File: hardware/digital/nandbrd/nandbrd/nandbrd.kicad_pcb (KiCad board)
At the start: 2 copper layers, 46.9 x 59.8 mm, 4 parts, among them J2 Conn_01x20_Male, U1 MT29F1G08ABAEAWP

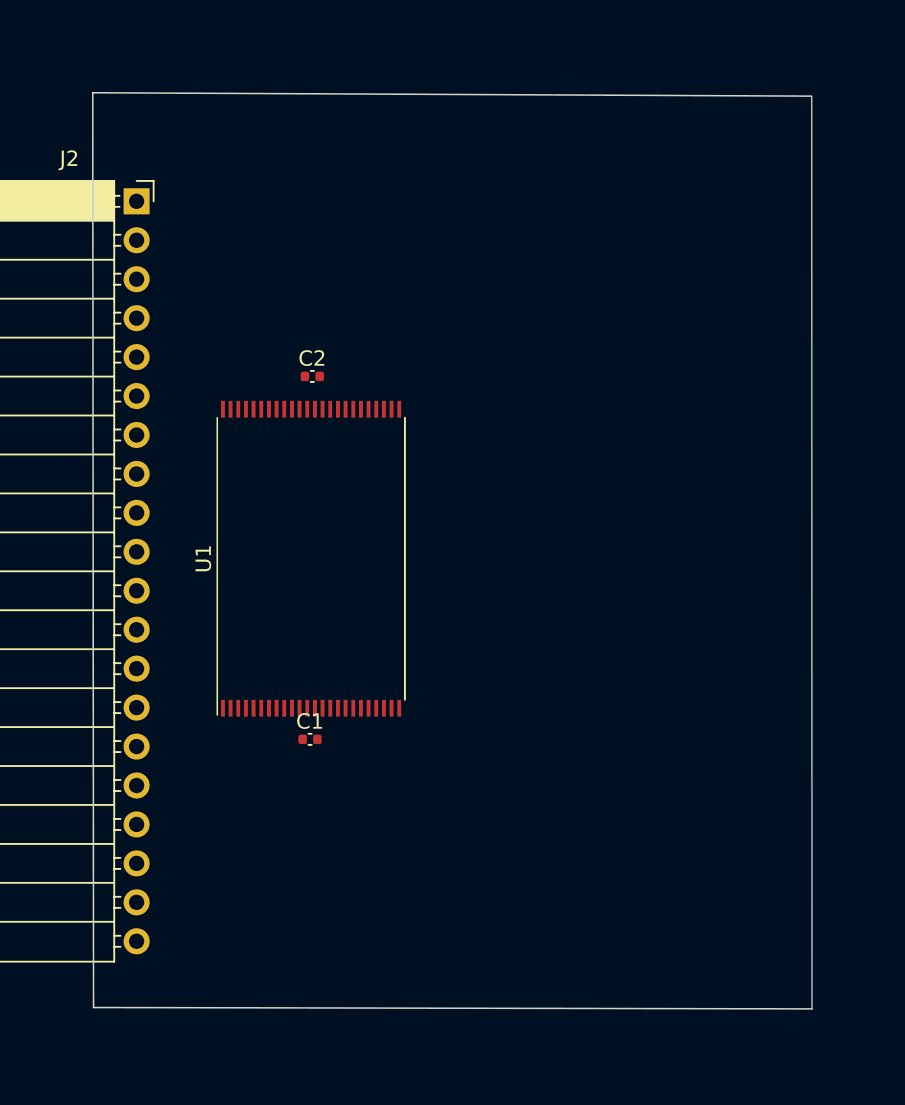
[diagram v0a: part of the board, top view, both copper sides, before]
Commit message: started NAND brd layout.
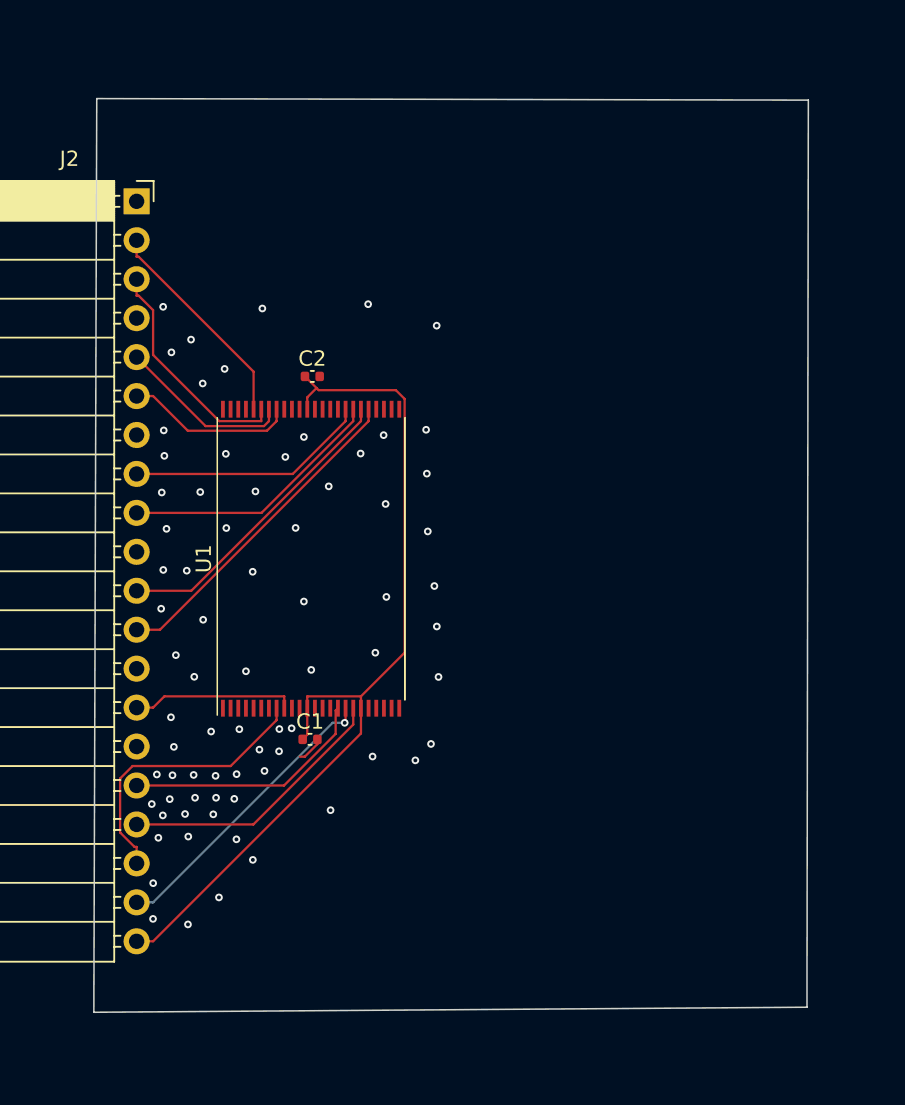
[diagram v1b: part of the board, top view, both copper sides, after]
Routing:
- net WP: track 0.00 -> 58.4 mm
- net D0: track 0.00 -> 21.5 mm
- net D1: track 0.00 -> 20.0 mm
- net ALE: track 0.00 -> 19.4 mm, vias 0 -> 1
- net RE: track 0.00 -> 18.6 mm
- net WE: track 0.00 -> 17.9 mm
- net D2: track 0.00 -> 17.4 mm
- net CLE: track 0.00 -> 16.1 mm
- net D3: track 0.00 -> 15.8 mm
- net D6: track 0.00 -> 15.1 mm
- net D7: track 0.00 -> 14.3 mm
- net D5: track 0.00 -> 11.4 mm
- net D4: track 0.00 -> 11.1 mm
- net CE: track 0.00 -> 10.7 mm
- net GND: track 0.00 -> 1.81 mm, vias 0 -> 75
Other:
- board size 46.9 x 59.8 mm -> 46.6 x 59.6 mm
